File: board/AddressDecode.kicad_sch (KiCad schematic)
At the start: 18 parts, among them U10 74LS154, U11 74F00, U12 74F86, U13 74F08, U14 74F32, U15 74F30, U16 74LS260, U17 74LS154, U18 74F04, U25 74F02

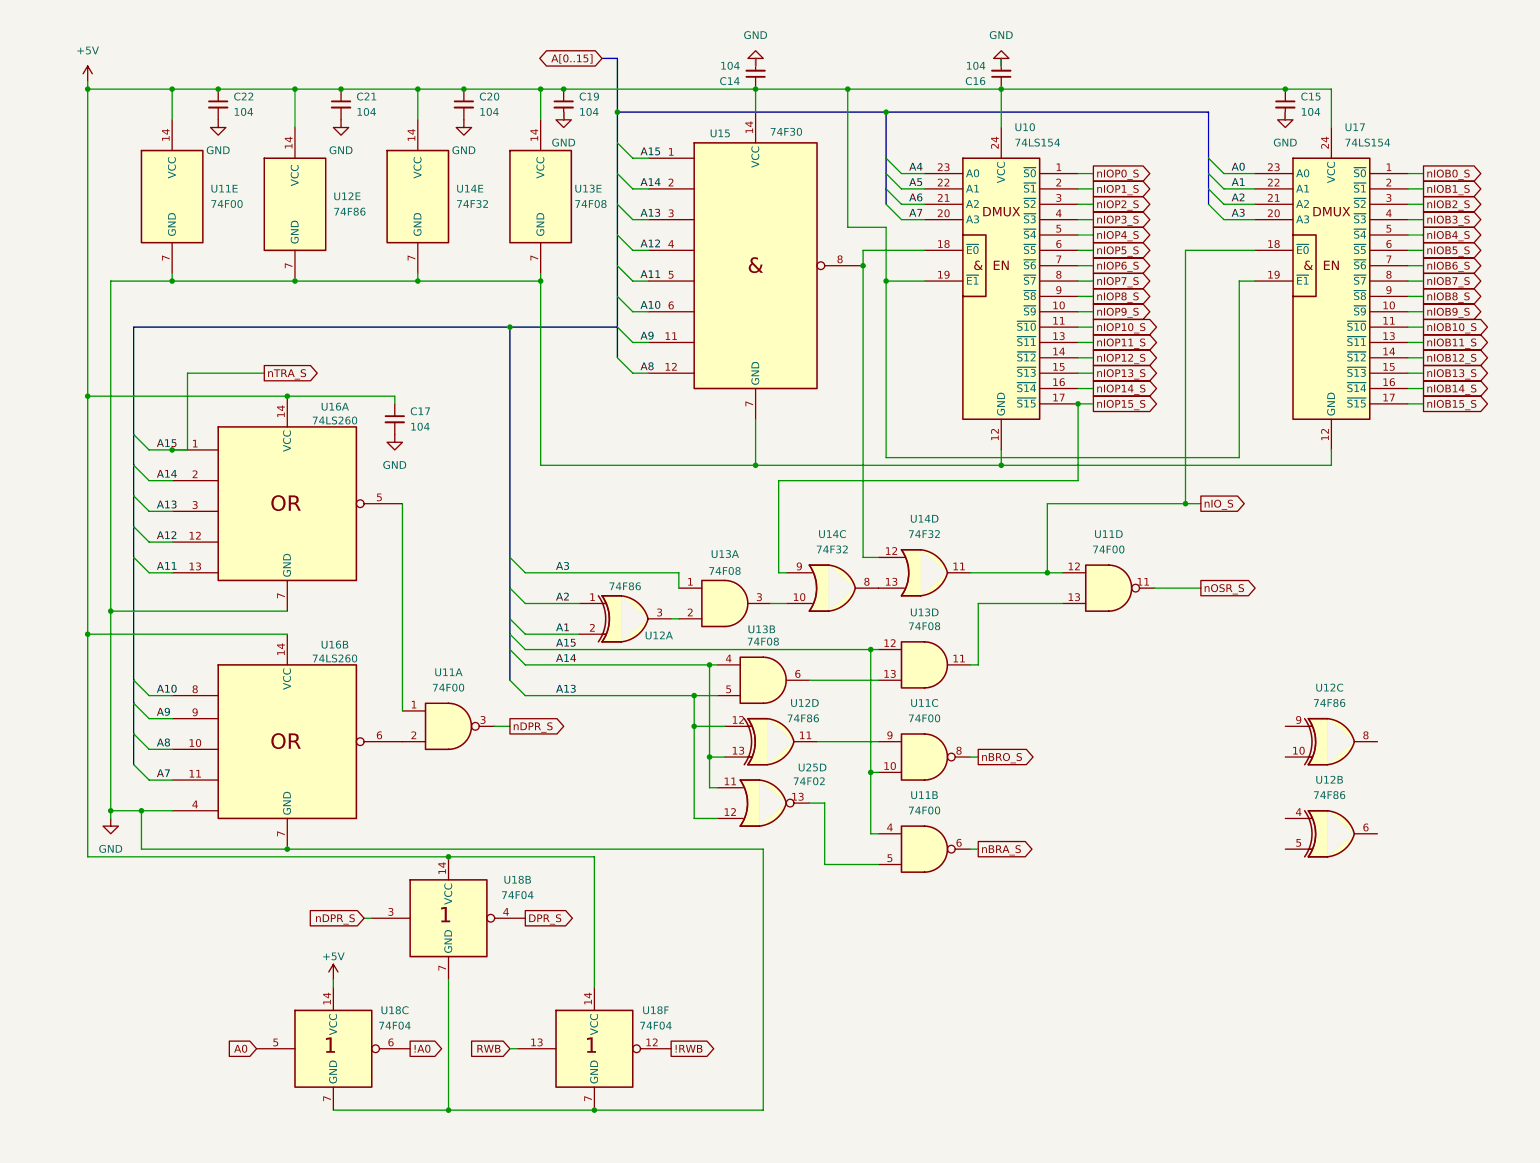
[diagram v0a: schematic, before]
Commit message: Added VIA port A header and voltage protection diode package socket. Updated logic.
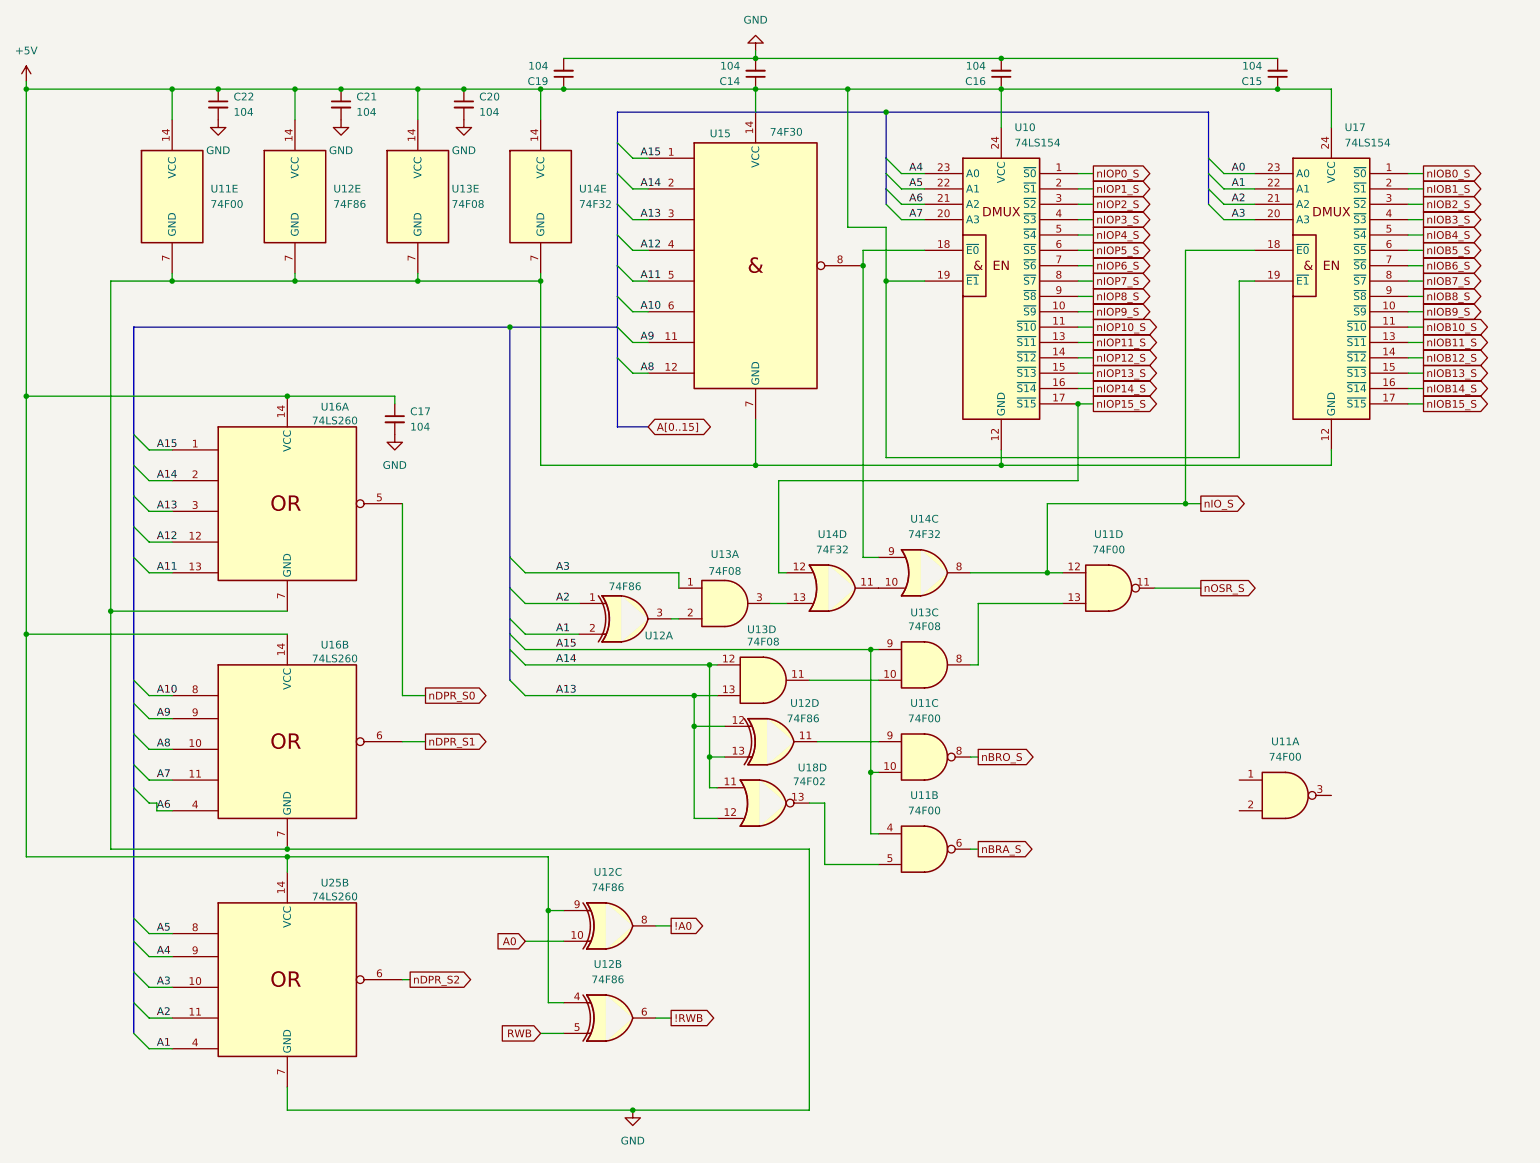
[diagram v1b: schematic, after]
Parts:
- removed U18: 74F04, Package_DIP:DIP-14_W7.62mm_Socket_LongPads, symbol 74xx_IEEE:7404
- added U25: 74LS260, Package_DIP:DIP-14_W7.62mm_Socket_LongPads, symbol 74xx_IEEE:7420
- renumbered U25 to U18
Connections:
- net !A0: now also U12.8
- net !RWB: now also U12.6
- net +5V: now also U12.4, U12.9, U25.14 (VCC)
- net A0: now also U12.10
- net A1: now also U25.4
- net A13: now also U13.13; no longer U13.5
- net A14: now also U13.12; no longer U13.4
- net A2: now also U25.11
- net A3: now also U25.10
- net A4: now also U25.9
- net A5: now also U25.8
- net A6: now also U16.4
- net GND: now also U25.7 (GND); no longer U16.4
- net RWB: now also U12.5
- net nIOP15_S: now also U14.12; no longer U14.9
- net nIO_S: now also U14.8; no longer U14.11
- net at U13.3: now also U14.13; no longer U14.10
- net at U11.1: no longer U16.5
- net at U11.2: no longer U16.6
- net at U11.13: now also U13.8; no longer U13.11
- net at U10.18 (~{E0}), U15.8: now also U14.9; no longer U14.12
- net nDPR_S: no longer names the net of U11.3
- net nTRA_S renamed A15
- net A15: now also U13.9; no longer U13.12
- new net: U13.10, U13.11
- new net: U14.10, U14.11
- new net nDPR_S0: U16.5
- new net nDPR_S1: U16.6
- new net nDPR_S2: U25.6
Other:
- moved on the sheet: C15, C19, U12B, U12C, U12E

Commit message: Initial production breakout card and main PCB versions
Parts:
- added C33: 104, Capacitor_THT:C_Disc_D5.0mm_W2.5mm_P5.00mm, symbol Device:C_Small
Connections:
- net +5V: now also C33.1
- net GND: now also C33.2
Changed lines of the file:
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@@
 		(title "Address Decode Logic")
 		(date "2024-10-09")
-		(rev "0.1A")
+		(rev "0.3B")
 		(company "Data Tuning")
 		(comment 1 "Hydra 16")
@@
 	)
 	(junction
+		(at 77.47 153.67)
+		(diameter 0)
+		(color 0 0 0 0)
+	)
+	(junction
 		(at 17.78 26.67)
 		(diameter 0)
@@
 	)
 	(bus_entry
-		(at 35.56 142.24)
+		(at 35.56 143.51)
 		(size 2.54 2.54)
 		(stroke
@@
 	(wire
 		(pts
-			(xy 80.01 173.99) (xy 81.28 173.99)
+			(xy 80.01 142.24) (xy 83.82 142.24)
 		)
 		(stroke
@@
 	(bus
 		(pts
-			(xy 35.56 138.43) (xy 35.56 142.24)
+			(xy 35.56 138.43) (xy 35.56 143.51)
 		)
 		(stroke
@@
 	(bus
 		(pts
-			(xy 35.56 142.24) (xy 35.56 163.83)
+			(xy 35.56 143.51) (xy 35.56 163.83)
 		)
 		(stroke
@@
 		)
 	)
-	(wire
-		(pts
-			(xy 39.37 146.05) (xy 41.91 146.05)
-		)
-		(stroke
-			(width 0)
-			(type default)
-		)
-	)
 	(bus
 		(pts
@@
 	(wire
 		(pts
+			(xy 80.01 142.24) (xy 80.01 173.99)
+		)
+		(stroke
+			(width 0)
+			(type default)
+		)
+	)
+	(wire
+		(pts
 			(xy 130.81 121.92) (xy 130.81 137.16)
 		)
@@
 	(wire
 		(pts
+			(xy 77.47 153.67) (xy 77.47 154.94)
+		)
+		(stroke
+			(width 0)
+			(type default)
+		)
+	)
+	(wire
+		(pts
 			(xy 194.31 45.72) (xy 191.77 45.72)
 		)
@@
 		)
 	)
+	(wire
+		(pts
+			(xy 77.47 153.67) (xy 60.96 153.67)
+		)
+		(stroke
+			(width 0)
+			(type default)
+		)
+	)
 	(bus
 		(pts
@@
 	(wire
 		(pts
-			(xy 39.37 144.78) (xy 39.37 146.05)
-		)
-		(stroke
-			(width 0)
-			(type default)
-		)
-	)
-	(wire
-		(pts
 			(xy 158.75 149.86) (xy 157.48 149.86)
 		)
@@
 	(wire
 		(pts
-			(xy 104.14 153.67) (xy 60.96 153.67)
+			(xy 104.14 153.67) (xy 77.47 153.67)
 		)
 		(stroke
@@
 	(wire
 		(pts
-			(xy 38.1 144.78) (xy 39.37 144.78)
+			(xy 38.1 146.05) (xy 41.91 146.05)
 		)
 		(stroke
@@
 	(global_label "nDPR_S2"
 		(shape output)
-		(at 81.28 173.99 0)
+		(at 83.82 142.24 0)
 		(fields_autoplaced yes)
 		(effects
@@
 		)
 		(property "Intersheetrefs" "${INTERSHEET_REFS}"
-			(at 92.6108 173.99 0)
+			(at 95.1508 142.24 0)
 			(effects
 				(font
@@
 	)
 	(symbol
+		(lib_id "Device:C_Small")
+		(at 77.47 157.48 0)
+		(unit 1)
+		(exclude_from_sim no)
+		(in_bom yes)
+		(on_board yes)
+		(dnp no)
+		(fields_autoplaced yes)
+		(property "Reference" "C33"
+			(at 80.01 156.2162 0)
+			(effects
+				(font
+					(size 1.27 1.27)
+				)
+				(justify left)
+			)
+		)
+		(property "Value" "104"
+			(at 80.01 158.7562 0)
+			(effects
+				(font
+					(size 1.27 1.27)
+				)
+				(justify left)
+			)
+		)
+		(property "Footprint" "Capacitor_THT:C_Disc_D5.0mm_W2.5mm_P5.00mm"
+			(at 77.47 157.48 0)
+			(effects
+				(font
+					(size 1.27 1.27)
+				)
+				(hide yes)
+			)
+		)
+		(property "Datasheet" "~"
+			(at 77.47 157.48 0)
+			(effects
+				(font
+					(size 1.27 1.27)
+				)
+				(hide yes)
+			)
+		)
+		(property "Description" "Unpolarized capacitor, small symbol"
+			(at 77.47 157.48 0)
+			(effects
+				(font
+					(size 1.27 1.27)
+				)
+				(hide yes)
+			)
+		)
+		(pin "1"
+		)
+		(pin "2"
+		)
+		(instances
+			(project "hydra-16"
+				(path "/ef29fc71-3fec-48b5-8a1a-46bee537a98c/e447d2ea-fe27-4cfd-bb5f-eaf105a9519f"
+					(reference "C33")
+					(unit 1)
+				)
+			)
+		)
+	)
+	(symbol
 		(lib_id "74xx:74LS32")
 		(at 151.13 109.22 0)
@@
 					(unit 1)
 				)
+			)
+		)
+	)
+	(symbol
+		(lib_id "power:GND")
+		(at 77.47 160.02 0)
+		(unit 1)
+		(exclude_from_sim no)
+		(in_bom yes)
+		(on_board yes)
+		(dnp no)
+		(fields_autoplaced yes)
+		(property "Reference" "#PWR021"
+			(at 77.47 166.37 0)
+			(effects
+				(font
+					(size 1.27 1.27)
+				)
+				(hide yes)
+			)
+		)
+		(property "Value" "GND"
+			(at 77.47 165.1 0)
+			(effects
+				(font
+					(size 1.27 1.27)
+				)
+			)
+		)
+		(property "Footprint" ""
+			(at 77.47 160.02 0)
+			(effects
+				(font
+					(size 1.27 1.27)
+				)
+				(hide yes)
+			)
+		)
+		(property "Datasheet" ""
+			(at 77.47 160.02 0)
+			(effects
+				(font
+					(size 1.27 1.27)
+				)
+				(hide yes)
+			)
+		)
+		(property "Description" "Power symbol creates a global label with name \"GND\" , ground"
+			(at 77.47 160.02 0)
+			(effects
+				(font
+					(size 1.27 1.27)
+				)
+				(hide yes)
+			)
+		)
+		(pin "1"
+		)
+		(instances
+			(project "hydra-16"
+				(path "/ef29fc71-3fec-48b5-8a1a-46bee537a98c/e447d2ea-fe27-4cfd-bb5f-eaf105a9519f"
+					(reference "#PWR021")
+					(unit 1)
+				)

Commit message: Version 0.4C of the routed board.
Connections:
- net +5V: no longer U10.19 (~{E1}), U17.19 (~{E1})
- net nIOP15_S: now also U14.9; no longer U14.12
- net nIO_S: now also U17.19 (~{E1})
- net at U10.18 (~{E0}), U15.8: now also U10.19 (~{E1}), U14.12; no longer U14.9
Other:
- moved on the sheet: U14C, U14D

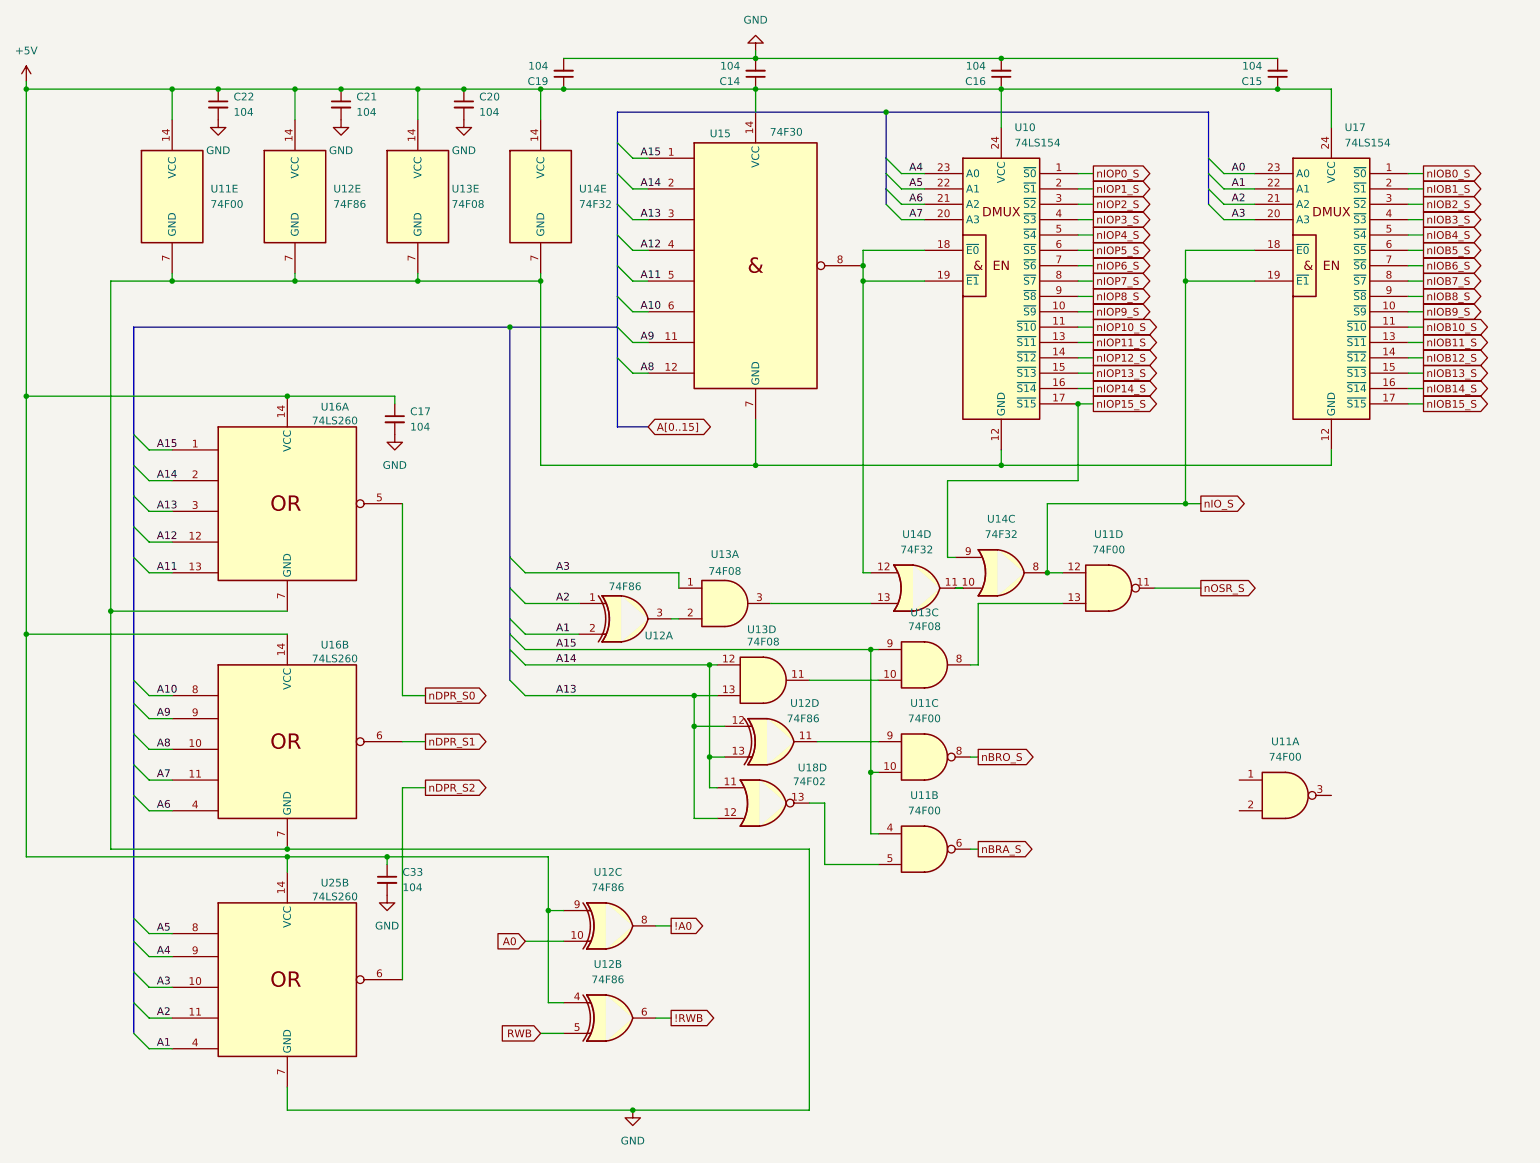
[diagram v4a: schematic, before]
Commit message: Version 0.5A of main board and updates to ROM code to match latest changes.
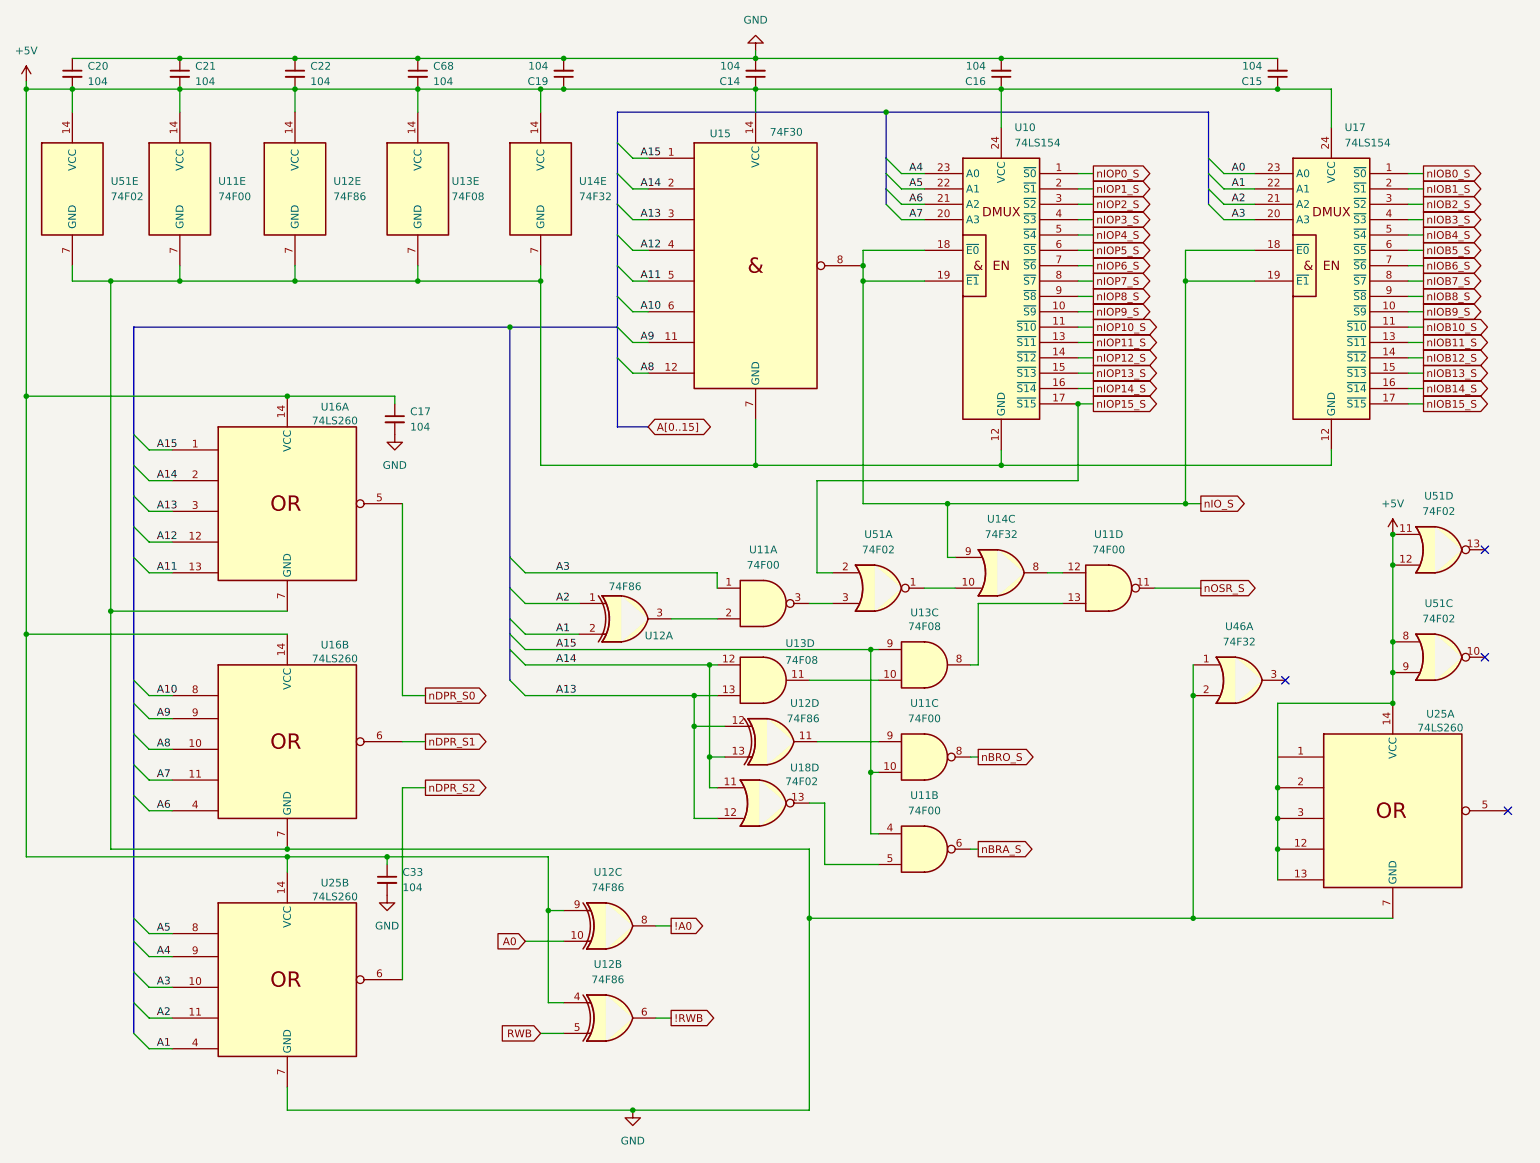
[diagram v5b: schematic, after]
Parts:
- removed unit 1 of U13
- removed unit 4 of U14
- added C68: 104, Capacitor_THT:C_Disc_D5.0mm_W2.5mm_P5.00mm, symbol Device:C_Small
- added unit 1 of U25
- added U46: 74F32, Package_DIP:DIP-14_W7.62mm_Socket_LongPads, symbol 74xx:74LS32
- added U51: 74F02, Package_DIP:DIP-14_W7.62mm_Socket_LongPads, symbol 74xx:7402
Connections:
- net +5V: now also C20.2, C21.2, C22.2, C68.2, U25.12, U25.13, U25.14 (VCC), U25.2, U25.3, U51.11, U51.12, U51.14 (VCC), U51.8, U51.9; no longer C20.1, C21.1, C22.1
- net A3: now also U11.1
- net GND: now also C20.1, C21.1, C22.1, C68.1, U25.7 (GND), U46.1, U46.2, U51.7 (GND); no longer C20.2, C21.2, C22.2
- net nIOP15_S: now also U51.2; no longer U14.9
- net nIO_S: now also U10.18 (~{E0}), U10.19 (~{E1}), U14.9, U15.8; no longer U11.12, U14.8
- net at U12.3: now also U11.2
- net at U14.10: now also U51.1
- net at U11.3: now also U51.3
- new net: U11.12, U14.8
- no-connect marks 0 -> 4
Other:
- moved on the sheet: U11E, U12E, U13E, U14E
